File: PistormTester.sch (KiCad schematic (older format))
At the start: 88 parts, among them J1 USB_B_Micro, J2 Conn_02x12_Odd_Even, J3 Conn_01x06_Female, J4 Conn_01x16_Female, J5 Conn_01x16_Female, J6 Conn_01x16_Female, J7 Conn_02x13_Odd_Even, J8 Conn_01x13, J9 Conn_01x02, U2 68000D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

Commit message: initial checkin
Rev A as sent to JLC on 19/06/21
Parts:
- C1: LCSC (none) -> C1525; LCSC part C1525 -> (none)
- C2: LCSC (none) -> C1548; LCSC part C1548 -> (none)
- D1, D10, D11, D12, D13, D14, D15, D16, D17, D18, D19, D2, D20, D21, D22, D23, D24, D3, D4, D5, D6, D7, D8, D9: LCSC (none) -> C72043; LCSC part C72043 -> (none)
- D25, D26, D27, D28, D29, D30, D31, D32, D33, D34, D35, D36, D37, D38, D39, D40, D47: LCSC (none) -> C72038; LCSC part C72038 -> (none)
- D41, D42, D43, D44, D45, D46, D48, D49, D50, D51, D52: LCSC (none) -> C72041; LCSC part C72041 -> (none)
- D53, D54, D55, D56, D57, D58: LCSC (none) -> C2286; LCSC part C2286 -> (none)
- D59, D60: LCSC (none) -> C2290; LCSC part C2290 -> (none)
- J1: LCSC (none) -> C145783; LCSC part C145783 -> (none)
- RN1, RN10, RN11, RN12, RN13, RN14, RN15, RN2, RN3, RN4, RN5, RN6, RN7, RN8, RN9: LCSC (none) -> C25726; LCSC part C25726 -> (none)
- X1: LCSC (none) -> C387338; LCSC part C387338 -> (none)

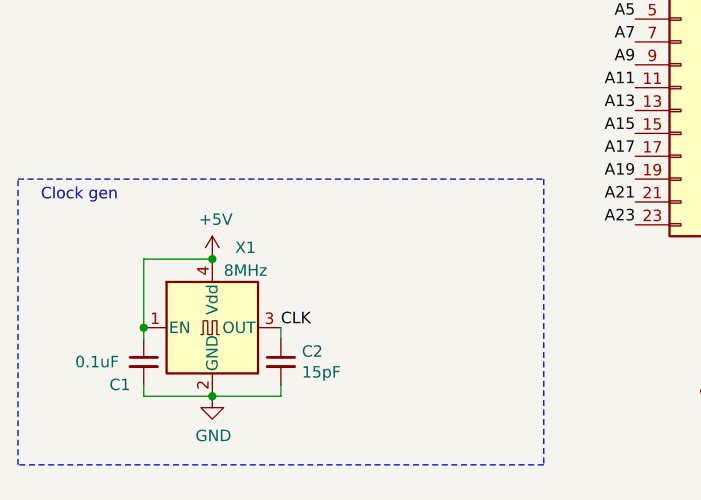
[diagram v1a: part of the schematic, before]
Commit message: Change to a 3.3v oscillator RevC.1
switched to a 3.3v Oscillator and an associated 3.3v regulator
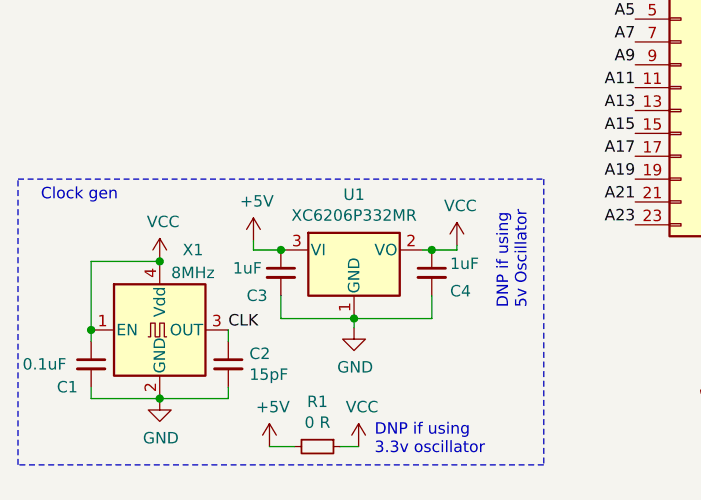
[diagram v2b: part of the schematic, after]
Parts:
- added C3, C4: 1uF, Capacitor_SMD:C_0402_1005Metric, symbol Device:C_Small
- added R1: 0 R, Resistor_SMD:R_0402_1005Metric, symbol Device:R_Small
- added U1: XC6206P332MR, Package_TO_SOT_SMD:SOT-23, symbol Regulator_Linear:AP2127N-1.0
- X1: LCSC C387338 -> C387336
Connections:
- net +5V: now also C3.1, R1.2, U1.3 (VI); no longer C1.1, X1.1 (EN), X1.4 (Vdd)
- net GND: now also C3.2, C4.2, U1.1 (GND)
- new net VCC: C1.1, C4.1, R1.1, U1.2 (VO), X1.1 (EN), X1.4 (Vdd)
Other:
- note added: "DNP if using \n3.3v oscillator"
- note added: "DNP if using \n5v Oscillator"
- moved on the sheet: C1, C2, X1
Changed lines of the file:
@@
 L Device:C_Small C2
 U 1 1 60FFEF5D
-P 1750 7250
-F 0 "C2" H 1842 7296 50  0000 L CNN
-F 1 "15pF" H 1842 7205 50  0000 L CNN
-F 2 "Capacitor_SMD:C_0402_1005Metric" H 1750 7250 50  0001 C CNN
-F 3 "~" H 1750 7250 50  0001 C CNN
-F 4 "C1548" H 1750 7250 50  0001 C CNN "LCSC"
-	1    1750 7250
-	1    0    0    -1
-$EndComp
-Wire Wire Line
-	1750 7400 1750 7350
+P 1520 7260
+F 0 "C2" H 1612 7306 50  0000 L CNN
+F 1 "15pF" H 1612 7215 50  0000 L CNN
+F 2 "Capacitor_SMD:C_0402_1005Metric" H 1520 7260 50  0001 C CNN
+F 3 "~" H 1520 7260 50  0001 C CNN
+F 4 "C1548" H 1520 7260 50  0001 C CNN "LCSC"
+	1    1520 7260
+	1    0    0    -1
+$EndComp
+Wire Wire Line
+	1520 7410 1520 7360
 $Comp
 L power:GND #PWR0103
 U 1 1 61049560
-P 1450 7400
-F 0 "#PWR0103" H 1450 7150 50  0001 C CNN
-F 1 "GND" H 1455 7227 50  0000 C CNN
-F 2 "" H 1450 7400 50  0001 C CNN
-F 3 "" H 1450 7400 50  0001 C CNN
-	1    1450 7400
-	1    0    0    -1
-$EndComp
-Connection ~ 1450 7400
-Wire Wire Line
-	1450 7400 1750 7400
+P 1220 7410
+F 0 "#PWR0103" H 1220 7160 50  0001 C CNN
+F 1 "GND" H 1225 7237 50  0000 C CNN
+F 2 "" H 1220 7410 50  0001 C CNN
+F 3 "" H 1220 7410 50  0001 C CNN
+	1    1220 7410
+	1    0    0    -1
+$EndComp
+Connection ~ 1220 7410
+Wire Wire Line
+	1220 7410 1520 7410
 Text Label 4300 1200 2    50   ~ 0
 CLK
@@
 L Oscillator:TXC-7C X1
 U 1 1 610E74E4
-P 1450 7100
-F 0 "X1" H 1550 7450 50  0000 L CNN
-F 1 "8MHz" H 1500 7350 50  0000 L CNN
-F 2 "Oscillator:Oscillator_SMD_EuroQuartz_XO32-4Pin_3.2x2.5mm" H 2150 6750 50  0001 C CNN
-F 3 "https://datasheet.lcsc.com/lcsc/1912111437_Shenzhen-SCTF-Elec-S3D8-000000A20F30T_C387338.pdf" H 1350 7100 50  0001 C CNN
-F 4 "C387338" H 1450 7100 50  0001 C CNN "LCSC"
-	1    1450 7100
-	1    0    0    -1
-$EndComp
-Wire Wire Line
-	1750 7150 1750 7100
-Text Label 1750 7100 0    50   ~ 0
+P 1220 7110
+F 0 "X1" H 1320 7460 50  0000 L CNN
+F 1 "8MHz" H 1270 7360 50  0000 L CNN
+F 2 "Oscillator:Oscillator_SMD_EuroQuartz_XO32-4Pin_3.2x2.5mm" H 1920 6760 50  0001 C CNN
+F 3 "https://datasheet.lcsc.com/lcsc/1912111437_Shenzhen-SCTF-Elec-S3D8-000000A20F30T_C387338.pdf" H 1120 7110 50  0001 C CNN
+F 4 "C387336" H 1220 7110 50  0001 C CNN "LCSC"
+	1    1220 7110
+	1    0    0    -1
+$EndComp
+Wire Wire Line
+	1520 7160 1520 7110
+Text Label 1520 7110 0    50   ~ 0
 CLK
-$Comp
-L power:+5V #PWR0104
-U 1 1 6110DC8B
-P 1450 6800
-F 0 "#PWR0104" H 1450 6650 50  0001 C CNN
-F 1 "+5V" H 1465 6973 50  0000 C CNN
-F 2 "" H 1450 6800 50  0001 C CNN
-F 3 "" H 1450 6800 50  0001 C CNN
-	1    1450 6800
-	1    0    0    -1
-$EndComp
-Wire Wire Line
-	1150 7100 1150 6800
-Wire Wire Line
-	1150 6800 1450 6800
-Connection ~ 1450 6800
+Wire Wire Line
+	920  7110 920  6810
+Wire Wire Line
+	920  6810 1220 6810
 $Comp
 L Connector:USB_B_Micro J1
@@
 L Device:C_Small C1
 U 1 1 61380C40
-P 1150 7250
-F 0 "C1" H 1000 7150 50  0000 L CNN
-F 1 "0.1uF" H 850 7250 50  0000 L CNN
-F 2 "Capacitor_SMD:C_0402_1005Metric" H 1150 7250 50  0001 C CNN
-F 3 "~" H 1150 7250 50  0001 C CNN
-F 4 "C1525" H 1150 7250 50  0001 C CNN "LCSC"
-	1    1150 7250
-	1    0    0    -1
-$EndComp
-Wire Wire Line
-	1150 7150 1150 7100
-Connection ~ 1150 7100
-Wire Wire Line
-	1150 7350 1150 7400
-Wire Wire Line
-	1150 7400 1450 7400
+P 920 7260
+F 0 "C1" H 770 7160 50  0000 L CNN
+F 1 "0.1uF" H 620 7260 50  0000 L CNN
+F 2 "Capacitor_SMD:C_0402_1005Metric" H 920 7260 50  0001 C CNN
+F 3 "~" H 920 7260 50  0001 C CNN
+F 4 "C1525" H 920 7260 50  0001 C CNN "LCSC"
+	1    920  7260
+	1    0    0    -1
+$EndComp
+Wire Wire Line
+	920  7160 920  7110
+Connection ~ 920  7110
+Wire Wire Line
+	920  7360 920  7410
+Wire Wire Line
+	920  7410 1220 7410
 Wire Wire Line
 	9050 6000 8950 6000
@@
 Text Notes 8750 5100 0    50   ~ 0
 Red
+$Comp
+L Regulator_Linear:AP2127N-1.0 U1
+U 1 1 611FADD6
+P 2070 6760
+F 0 "U1" H 2070 7002 50  0000 C CNN
+F 1 "XC6206P332MR" H 2070 6911 50  0000 C CNN
+F 2 "Package_TO_SOT_SMD:SOT-23" H 2070 6985 50  0001 C CIN
+F 3 "https://www.diodes.com/assets/Datasheets/AP2127.pdf" H 2070 6760 50  0001 C CNN
+F 4 "C5446" H 2070 6760 50  0001 C CNN "LCSC"
+	1    2070 6760
+	1    0    0    -1
+$EndComp
+$Comp
+L power:VCC #PWR0104
+U 1 1 612041A0
+P 1220 6810
+F 0 "#PWR0104" H 1220 6660 50  0001 C CNN
+F 1 "VCC" H 1235 6983 50  0000 C CNN
+F 2 "" H 1220 6810 50  0001 C CNN
+F 3 "" H 1220 6810 50  0001 C CNN
+	1    1220 6810
+	1    0    0    -1
+$EndComp
+Connection ~ 1220 6810
+$Comp
+L power:+5V #PWR0109
+U 1 1 6120C795
+P 1630 6720
+F 0 "#PWR0109" H 1630 6570 50  0001 C CNN
+F 1 "+5V" H 1645 6893 50  0000 C CNN
+F 2 "" H 1630 6720 50  0001 C CNN
+F 3 "" H 1630 6720 50  0001 C CNN
+	1    1630 6720
+	1    0    0    -1
+$EndComp
+Wire Wire Line
+	1630 6720 1630 6760
+Wire Wire Line
+	1630 6760 1750 6760
+Wire Wire Line
+	2370 6760 2410 6760
+Wire Wire Line
+	2520 6760 2520 6740
+$Comp
+L power:VCC #PWR0110
+U 1 1 61228A7D
+P 2520 6740
+F 0 "#PWR0110" H 2520 6590 50  0001 C CNN
+F 1 "VCC" H 2535 6913 50  0000 C CNN
+F 2 "" H 2520 6740 50  0001 C CNN
+F 3 "" H 2520 6740 50  0001 C CNN
+	1    2520 6740
+	1    0    0    -1
+$EndComp
+$Comp
+L power:GND #PWR0111
+U 1 1 6122BC8C
+P 2070 7100
+F 0 "#PWR0111" H 2070 6850 50  0001 C CNN
+F 1 "GND" H 2075 6927 50  0000 C CNN
+F 2 "" H 2070 7100 50  0001 C CNN
+F 3 "" H 2070 7100 50  0001 C CNN
+	1    2070 7100
+	1    0    0    -1
+$EndComp
+$Comp
+L power:+5V #PWR0112
+U 1 1 61295288
+P 1700 7620
+F 0 "#PWR0112" H 1700 7470 50  0001 C CNN
+F 1 "+5V" H 1715 7793 50  0000 C CNN
+F 2 "" H 1700 7620 50  0001 C CNN
+F 3 "" H 1700 7620 50  0001 C CNN
+	1    1700 7620
+	1    0    0    -1
+$EndComp
+$Comp
+L power:VCC #PWR0113
+U 1 1 61295D0D
+P 2090 7620
+F 0 "#PWR0113" H 2090 7470 50  0001 C CNN
+F 1 "VCC" H 2105 7793 50  0000 C CNN
+F 2 "" H 2090 7620 50  0001 C CNN
+F 3 "" H 2090 7620 50  0001 C CNN
+	1    2090 7620
+	1    0    0    -1
+$EndComp
+$Comp
+L Device:R_Small R1
+U 1 1 61296EBD
+P 1910 7620
+F 0 "R1" V 1714 7620 50  0000 C CNN
+F 1 "0 R" V 1805 7620 50  0000 C CNN
+F 2 "Resistor_SMD:R_0402_1005Metric" H 1910 7620 50  0001 C CNN
+F 3 "~" H 1910 7620 50  0001 C CNN
+F 4 "C17168" H 1910 7620 50  0001 C CNN "LCSC"
+	1    1910 7620
+	0    1    1    0
+$EndComp
+Wire Wire Line
+	2090 7620 2010 7620
+Wire Wire Line
+	1810 7620 1700 7620
+Text Notes 2160 7660 0    50   ~ 0
+DNP if using \n3.3v oscillator
+Text Notes 2830 7020 1    50   ~ 0
+DNP if using \n5v Oscillator
+$Comp
+L Device:C_Small C3
+U 1 1 61301B5C
+P 1750 6860
+F 0 "C3" H 1600 6760 50  0000 L CNN
+F 1 "1uF" H 1540 6880 50  0000 L CNN
+F 2 "Capacitor_SMD:C_0402_1005Metric" H 1750 6860 50  0001 C CNN
+F 3 "~" H 1750 6860 50  0001 C CNN
+F 4 "C52923" H 1750 6860 50  0001 C CNN "LCSC"
+	1    1750 6860
+	1    0    0    -1
+$EndComp
+Connection ~ 1750 6760
+Wire Wire Line
+	1750 6760 1770 6760
+Wire Wire Line
+	2070 7060 1750 7060
+Wire Wire Line
+	1750 7060 1750 6960
+Wire Wire Line
+	2070 7100 2070 7060
+Connection ~ 2070 7060
+$Comp
+L Device:C_Small C4
+U 1 1 6132C578
+P 2410 6860
+F 0 "C4" H 2490 6780 50  0000 L CNN
+F 1 "1uF" H 2490 6900 50  0000 L CNN
+F 2 "Capacitor_SMD:C_0402_1005Metric" H 2410 6860 50  0001 C CNN
+F 3 "~" H 2410 6860 50  0001 C CNN
+F 4 "C52923" H 2410 6860 50  0001 C CNN "LCSC"
+	1    2410 6860
+	1    0    0    -1
+$EndComp
+Connection ~ 2410 6760
+Wire Wire Line
+	2410 6760 2520 6760
+Wire Wire Line
+	2410 6960 2410 7060
+Wire Wire Line
+	2410 7060 2070 7060
 $EndSCHEMATC
